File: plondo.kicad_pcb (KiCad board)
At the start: 2 copper layers, 126 parts, among them J1 AVR_TC2030, J2 USB4085, SW0 MX_SW_HS, SW1 MX_SW_HS, SW10 MX_SW_HS, SW11 MX_SW_HS, SW12 MX_SW_HS, SW13 MX_SW_HS, SW14 MX_SW_HS, SW15 MX_SW_HS, SW16 MX_SW_HS, SW17 MX_SW_HS, SW18 MX_SW_HS, SW19 MX_SW_HS, SW2 MX_SW_HS, SW20 MX_SW_HS, SW21 MX_SW_HS, SW22 MX_SW_HS, SW23 MX_SW_HS, SW24 MX_SW_HS, SW25 MX_SW_HS, SW26 MX_SW_HS, SW27 MX_SW_HS, SW28 MX_SW_HS, SW29 MX_SW_HS, SW3 MX_SW_HS, SW30 MX_SW_HS, SW31 MX_SW_HS, SW32 MX_SW_HS, SW33 MX_SW_HS, SW34 MX_SW_HS, SW35 MX_SW_HS, SW36 MX_SW_HS, SW37 MX_SW_HS, SW38 MX_SW_HS, SW39 MX_SW_HS, SW4 MX_SW_HS, SW40 MX_SW_HS, SW41 MX_SW_HS, SW42 MX_SW_HS, SW43 MX_SW_HS, SW44 MX_SW_HS, SW45 MX_SW_HS, SW46 MX_SW_HS, SW47 MX_SW_HS, SW5 MX_SW_HS, SW6 MX_SW_HS, SW7 MX_SW_HS, SW8 MX_SW_HS, SW9 MX_SW_HS, U1 ATmega32A-P, Y1 Crystal

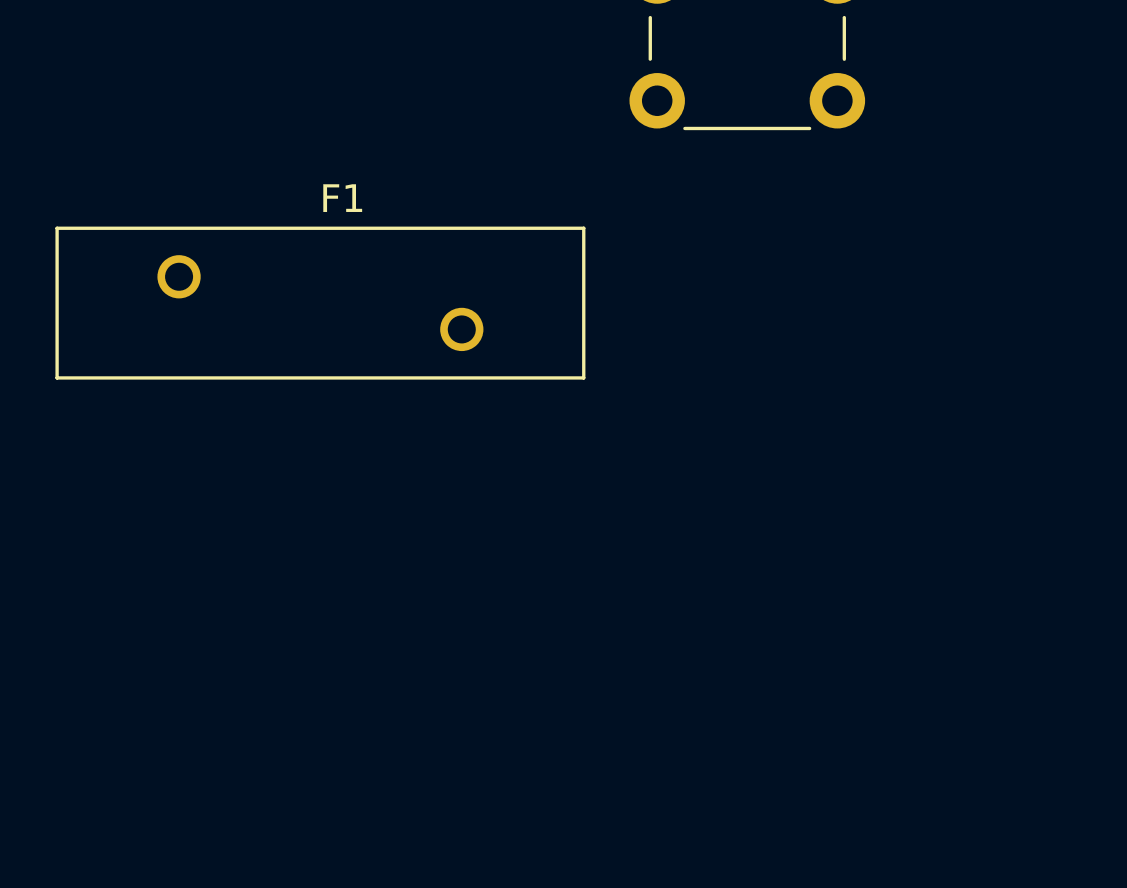
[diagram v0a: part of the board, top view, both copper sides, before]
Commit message: add pullups for i2c lines
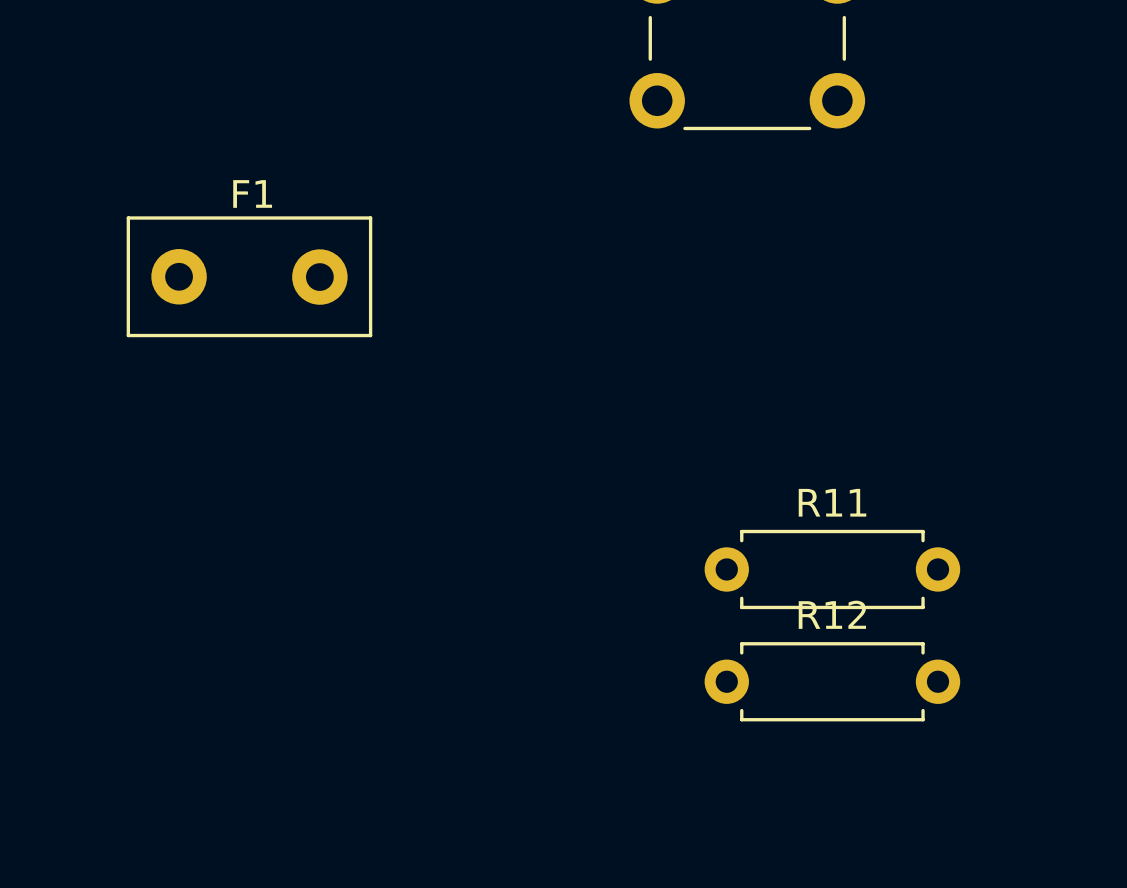
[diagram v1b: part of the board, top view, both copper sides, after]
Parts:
- added R11: 10k, Resistor_THT:R_Axial_DIN0207_L6.3mm_D2.5mm_P7.62mm_Horizontal, F.Cu at (-38.1, 114.3)
- added R12: 10k, Resistor_THT:R_Axial_DIN0207_L6.3mm_D2.5mm_P7.62mm_Horizontal, F.Cu at (-38.1, 118.3)
- F1: footprint Fuse:Fuse_BelFuse_0ZRE0100FF_L18.7mm_W5.1mm -> Fuse:Fuse_Littelfuse_395Series
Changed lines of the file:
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@@
     )
   )
+  (footprint "Resistor_THT:R_Axial_DIN0207_L6.3mm_D2.5mm_P7.62mm_Horizontal" (layer "F.Cu")
+    (at -38.1 114.3)
+    (descr "Resistor, Axial_DIN0207 series, Axial, Horizontal, pin pitch=7.62mm, 0.25W = 1/4W, length*diameter=6.3*2.5mm^2, http://cdn-reichelt.de/documents/datenblatt/B400/1_4W%23YAG.pdf")
+    (tags "Resistor Axial_DIN0207 series Axial Horizontal pin pitch 7.62mm 0.25W = 1/4W length 6.3mm diameter 2.5mm")
+    (property "Sheetfile" "plondo.kicad_sch")
+    (property "Sheetname" "")
+    (attr through_hole)
+    (fp_text reference "R11" (at 3.81 -2.37) (layer "F.SilkS")
+      (effects (font (size 1 1) (thickness 0.15)))
+    )
+    (fp_text value "10k" (at 3.81 2.37) (layer "F.Fab")
+      (effects (font (size 1 1) (thickness 0.15)))
+    )
+    (fp_text user "${REFERENCE}" (at 3.81 0) (layer "F.Fab")
+      (effects (font (size 1 1) (thickness 0.15)))
+    )
+    (fp_line (start 7.08 1.37) (end 7.08 1.04) (layer "F.SilkS") (width 0.12))
+    (fp_line (start 0.54 -1.04) (end 0.54 -1.37) (layer "F.SilkS") (width 0.12))
+    (fp_line (start 0.54 1.04) (end 0.54 1.37) (layer "F.SilkS") (width 0.12))
+    (fp_line (start 7.08 -1.37) (end 7.08 -1.04) (layer "F.SilkS") (width 0.12))
+    (fp_line (start 0.54 1.37) (end 7.08 1.37) (layer "F.SilkS") (width 0.12))
+    (fp_line (start 0.54 -1.37) (end 7.08 -1.37) (layer "F.SilkS") (width 0.12))
+    (fp_line (start 8.67 -1.5) (end -1.05 -1.5) (layer "F.CrtYd") (width 0.05))
+    (fp_line (start -1.05 1.5) (end 8.67 1.5) (layer "F.CrtYd") (width 0.05))
+    (fp_line (start 8.67 1.5) (end 8.67 -1.5) (layer "F.CrtYd") (width 0.05))
+    (fp_line (start -1.05 -1.5) (end -1.05 1.5) (layer "F.CrtYd") (width 0.05))
+    (fp_line (start 6.96 -1.25) (end 0.66 -1.25) (layer "F.Fab") (width 0.1))
+    (fp_line (start 6.96 1.25) (end 6.96 -1.25) (layer "F.Fab") (width 0.1))
+    (fp_line (start 7.62 0) (end 6.96 0) (layer "F.Fab") (width 0.1))
+    (fp_line (start 0.66 -1.25) (end 0.66 1.25) (layer "F.Fab") (width 0.1))
+    (fp_line (start 0.66 1.25) (end 6.96 1.25) (layer "F.Fab") (width 0.1))
+    (fp_line (start 0 0) (end 0.66 0) (layer "F.Fab") (width 0.1))
+    (pad "1" thru_hole circle (at 0 0) (size 1.6 1.6) (drill 0.8) (layers *.Cu *.Mask)
+      (net 5 "VCC") (pintype "passive"))
+    (pad "2" thru_hole oval (at 7.62 0) (size 1.6 1.6) (drill 0.8) (layers *.Cu *.Mask)
+      (net 76 "SDA") (pintype "passive"))
+    (model "${KICAD6_3DMODEL_DIR}/Resistor_THT.3dshapes/R_Axial_DIN0207_L6.3mm_D2.5mm_P7.62mm_Horizontal.wrl"
+      (offset (xyz 0 0 0))
+      (scale (xyz 1 1 1))
+      (rotate (xyz 0 0 0))
+    )
+  )
   (footprint "Diode_THT:D_DO-35_SOD27_P7.62mm_Horizontal" (layer "F.Cu")
     (at 137.16 45.72 -90)
@@
     )
   )
+  (footprint "Resistor_THT:R_Axial_DIN0207_L6.3mm_D2.5mm_P7.62mm_Horizontal" (layer "F.Cu")
+    (at -38.1 118.35)
+    (descr "Resistor, Axial_DIN0207 series, Axial, Horizontal, pin pitch=7.62mm, 0.25W = 1/4W, length*diameter=6.3*2.5mm^2, http://cdn-reichelt.de/documents/datenblatt/B400/1_4W%23YAG.pdf")
+    (tags "Resistor Axial_DIN0207 series Axial Horizontal pin pitch 7.62mm 0.25W = 1/4W length 6.3mm diameter 2.5mm")
+    (property "Sheetfile" "plondo.kicad_sch")
+    (property "Sheetname" "")
+    (attr through_hole)
+    (fp_text reference "R12" (at 3.81 -2.37) (layer "F.SilkS")
+      (effects (font (size 1 1) (thickness 0.15)))
+    )
+    (fp_text value "10k" (at 3.81 2.37) (layer "F.Fab")
+      (effects (font (size 1 1) (thickness 0.15)))
+    )
+    (fp_text user "${REFERENCE}" (at 3.81 0) (layer "F.Fab")
+      (effects (font (size 1 1) (thickness 0.15)))
+    )
+    (fp_line (start 7.08 1.37) (end 7.08 1.04) (layer "F.SilkS") (width 0.12))
+    (fp_line (start 0.54 -1.37) (end 7.08 -1.37) (layer "F.SilkS") (width 0.12))
+    (fp_line (start 0.54 1.04) (end 0.54 1.37) (layer "F.SilkS") (width 0.12))
+    (fp_line (start 7.08 -1.37) (end 7.08 -1.04) (layer "F.SilkS") (width 0.12))
+    (fp_line (start 0.54 -1.04) (end 0.54 -1.37) (layer "F.SilkS") (width 0.12))
+    (fp_line (start 0.54 1.37) (end 7.08 1.37) (layer "F.SilkS") (width 0.12))
+    (fp_line (start -1.05 1.5) (end 8.67 1.5) (layer "F.CrtYd") (width 0.05))
+    (fp_line (start 8.67 1.5) (end 8.67 -1.5) (layer "F.CrtYd") (width 0.05))
+    (fp_line (start -1.05 -1.5) (end -1.05 1.5) (layer "F.CrtYd") (width 0.05))
+    (fp_line (start 8.67 -1.5) (end -1.05 -1.5) (layer "F.CrtYd") (width 0.05))
+    (fp_line (start 0.66 1.25) (end 6.96 1.25) (layer "F.Fab") (width 0.1))
+    (fp_line (start 6.96 1.25) (end 6.96 -1.25) (layer "F.Fab") (width 0.1))
+    (fp_line (start 7.62 0) (end 6.96 0) (layer "F.Fab") (width 0.1))
+    (fp_line (start 0.66 -1.25) (end 0.66 1.25) (layer "F.Fab") (width 0.1))
+    (fp_line (start 0 0) (end 0.66 0) (layer "F.Fab") (width 0.1))
+    (fp_line (start 6.96 -1.25) (end 0.66 -1.25) (layer "F.Fab") (width 0.1))
+    (pad "1" thru_hole circle (at 0 0) (size 1.6 1.6) (drill 0.8) (layers *.Cu *.Mask)
+      (net 5 "VCC") (pintype "passive"))
+    (pad "2" thru_hole oval (at 7.62 0) (size 1.6 1.6) (drill 0.8) (layers *.Cu *.Mask)
+      (net 77 "SCL") (pintype "passive"))
+    (model "${KICAD6_3DMODEL_DIR}/Resistor_THT.3dshapes/R_Axial_DIN0207_L6.3mm_D2.5mm_P7.62mm_Horizontal.wrl"
+      (offset (xyz 0 0 0))
+      (scale (xyz 1 1 1))
+      (rotate (xyz 0 0 0))
+    )
+  )
   (footprint "Capacitor_THT:C_Disc_D7.5mm_W4.4mm_P5.00mm" (layer "F.Cu")
     (at -20.37 61.65)
@@
     )
   )
-  (footprint "Fuse:Fuse_BelFuse_0ZRE0100FF_L18.7mm_W5.1mm" (layer "F.Cu")
+  (footprint "Fuse:Fuse_Littelfuse_395Series" (layer "F.Cu")
     (at -57.86 103.74)
-    (descr "Fuse 0ZRE0100FF, BelFuse, Radial Leaded PTC,https://www.belfuse.com/resources/datasheets/circuitprotection/ds-cp-0zre-series.pdf")
-    (tags "0ZRE BelFuse radial PTC")
+    (descr "Fuse, TE5, Littelfuse/Wickmann, No. 460, No560,")
+    (tags "Fuse TE5 Littelfuse/Wickmann No. 460 No560 ")
     (property "Sheetfile" "plondo.kicad_sch")
     (property "Sheetname" "")
     (attr through_hole)
-    (fp_text reference "F1" (at 5.9 -2.8) (layer "F.SilkS")
+    (fp_text reference "F1" (at 2.65 -2.95) (layer "F.SilkS")
       (effects (font (size 1 1) (thickness 0.15)))
     )
-    (fp_text value "500mA" (at 5.6 5.2) (layer "F.Fab")
+    (fp_text value "500mA" (at 2.35 3.1) (layer "F.Fab")
       (effects (font (size 1 1) (thickness 0.15)))
     )
-    (fp_text user "${REFERENCE}" (at 5.7 0.4) (layer "F.Fab")
+    (fp_text user "${REFERENCE}" (at 2.75 -1.25) (layer "F.Fab")
       (effects (font (size 1 1) (thickness 0.15)))
     )
-    (fp_line (start -4.4 -1.75) (end -4.4 3.65) (layer "F.SilkS") (width 0.12))
-    (fp_line (start -4.4 3.65) (end 14.6 3.65) (layer "F.SilkS") (width 0.12))
-    (fp_line (start 14.6 -1.75) (end 14.6 3.65) (layer "F.SilkS") (width 0.12))
-    (fp_line (start -4.4 -1.75) (end 14.6 -1.75) (layer "F.SilkS") (width 0.12))
-    (fp_line (start -4.5 -1.85) (end 14.7 -1.85) (layer "F.CrtYd") (width 0.05))
-    (fp_line (start -4.5 3.75) (end 14.7 3.75) (layer "F.CrtYd") (width 0.05))
-    (fp_line (start -4.5 -1.85) (end -4.5 3.75) (layer "F.CrtYd") (width 0.05))
-    (fp_line (start 14.7 -1.85) (end 14.7 3.75) (layer "F.CrtYd") (width 0.05))
-    (fp_line (start -4.25 -1.6) (end -4.25 3.5) (layer "F.Fab") (width 0.1))
-    (fp_line (start -4.25 -1.6) (end 14.45 -1.6) (layer "F.Fab") (width 0.1))
-    (fp_line (start -4.25 3.5) (end 14.45 3.5) (layer "F.Fab") (width 0.1))
-    (fp_line (start 14.45 -1.6) (end 14.45 3.5) (layer "F.Fab") (width 0.1))
-    (pad "1" thru_hole circle (at 0 0) (size 1.56 1.56) (drill 1.01) (layers *.Cu *.Mask)
+    (fp_line (start 6.91 2.12) (end 6.91 -2.12) (layer "F.SilkS") (width 0.12))
+    (fp_line (start -1.83 -2.12) (end -1.83 2.12) (layer "F.SilkS") (width 0.12))
+    (fp_line (start -1.83 -2.12) (end 6.91 -2.12) (layer "F.SilkS") (width 0.12))
+    (fp_line (start 6.91 2.12) (end -1.83 2.12) (layer "F.SilkS") (width 0.12))
+    (fp_line (start 7.04 2.25) (end 7.04 -2.25) (layer "F.CrtYd") (width 0.05))
+    (fp_line (start -1.96 -2.25) (end -1.96 2.25) (layer "F.CrtYd") (width 0.05))
+    (fp_line (start -1.96 -2.25) (end 7.04 -2.25) (layer "F.CrtYd") (width 0.05))
+    (fp_line (start 7.04 2.25) (end -1.96 2.25) (layer "F.CrtYd") (width 0.05))
+    (fp_line (start -1.71 -2) (end -1.71 2) (layer "F.Fab") (width 0.1))
+    (fp_line (start 6.79 2) (end 6.79 -2) (layer "F.Fab") (width 0.1))
+    (fp_line (start 6.79 -2) (end -1.71 -2) (layer "F.Fab") (width 0.1))
+    (fp_line (start -1.71 2) (end 6.79 2) (layer "F.Fab") (width 0.1))
+    (pad "1" thru_hole circle (at 0 0) (size 2 2) (drill 1) (layers *.Cu *.Mask)
       (net 60 "Net-(F1-Pad1)") (pintype "passive"))
-    (pad "2" thru_hole circle (at 10.2 1.9) (size 1.56 1.56) (drill 1.01) (layers *.Cu *.Mask)
+    (pad "2" thru_hole circle (at 5.08 0.01) (size 2 2) (drill 1) (layers *.Cu *.Mask)
       (net 5 "VCC") (pintype "passive"))
-    (model "${KICAD6_3DMODEL_DIR}/Fuse.3dshapes/Fuse_BelFuse_0ZRE_0ZRE0100FF_L18.7mm_W5.1mm.wrl"
+    (model "${KICAD6_3DMODEL_DIR}/Fuse.3dshapes/Fuse_Littelfuse_395Series.wrl"
       (offset (xyz 0 0 0))
       (scale (xyz 1 1 1))

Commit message: edited schematics for clarity, position more of pcb
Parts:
- moved F1 308.8 mm to (246.4, 50.8), turned to 90 degrees
- moved C5 275.7 mm to (232.4, 45.8), turned to -90 degrees
- moved C3 273.0 mm to (241.3, 48.3), turned to 90 degrees
- moved J2 263.8 mm to (243.8, 39.6)
- moved C4 244.1 mm to (236.2, 50.8), turned to 90 degrees
- moved BSW1 235.8 mm to (183.4, 19.3)
- moved Y1 220.8 mm to (180.3, 38.1)
- moved RSW1 211.9 mm to (172.0, 19.3)
- moved C2 211.9 mm to (190.5, 40.6), turned to 90 degrees
- moved C1 209.1 mm to (175.3, 35.6), turned to -90 degrees
- moved D48 47.0 mm to (221.0, 47.0), turned to -90 degrees
- moved D49 44.5 mm to (218.4, 47.0), turned to -90 degrees
- moved U1 30.5 mm to (212.1, 43.2)

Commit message: position all components on the pcb
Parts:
- J1: value AVR_TC2030 -> AVR ISP
- moved R3 271.4 mm to (240.0, 62.2)
- moved R6 260.1 mm to (215.9, 54.6)
- moved R4 259.6 mm to (215.9, 47.0)
- moved R5 248.4 mm to (215.9, 50.8)
- moved R2 247.9 mm to (240.0, 58.4)
- moved R1 212.2 mm to (179.1, 33.0)
- moved J1 179.1 mm to (163.8, 35.6), turned to 90 degrees
- moved R12 127.3 mm to (59.7, 36.8)
- moved R11 122.4 mm to (59.7, 40.6)
- moved OL1 102.5 mm to (72.4, 41.9), turned to 90 degrees
- moved R9 90.9 mm to (45.7, 41.9), turned to 90 degrees
- moved R7 86.9 mm to (35.6, 41.9), turned to 90 degrees
- moved R10 75.0 mm to (50.8, 41.9), turned to 90 degrees
- moved LED2 74.9 mm to (40.6, 31.8), turned to 90 degrees
- moved R8 73.5 mm to (40.6, 41.9), turned to 90 degrees
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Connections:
- net XTAL1 renamed Net-(U1-Pad13)
- net XTAL2 renamed Net-(U1-Pad12)

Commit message: rearrange pins + misc pcb arrangement fixes
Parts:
- added Ref**: Val**, kbd:spacer_m2, F.Cu at (48.3, 83.8)
- added Ref**: Val**, kbd:spacer_m2, F.Cu at (251.5, 83.8)
- added Ref**: Val**, kbd:spacer_m2, F.Cu at (251.5, 124.5)
- added Ref**: Val**, kbd:spacer_m2, F.Cu at (48.3, 124.5)
- J1: footprint Connector_PinHeader_1.27mm:PinHeader_2x03_P1.27mm_Vertical -> Connector_PinHeader_2.54mm:PinHeader_2x03_P2.54mm_Vertical
- OL1: footprint kbd:OLED_1side -> kbd:OLED_v2
- SW0, SW1, SW10, SW11, SW12, SW13, SW14, SW15, SW16, SW17, SW18, SW19, SW2, SW20, SW21, SW22, SW23, SW24, SW25, SW26, SW27, SW28, SW29, SW3, SW30, SW31, SW32, SW33, SW34, SW35, SW36, SW37, SW38, SW39, SW4, SW40, SW41, SW42, SW43, SW44, SW45, SW46, SW47, SW5, SW6, SW7, SW8, SW9: moved to B.Cu
- Y1: value Crystal -> 16MHz
- moved LED1 202.0 mm to (236.2, 55.2), turned to 180 degrees
- moved R7 185.9 mm to (221.0, 55.9), turned to 0 degrees
- moved R8 124.7 mm to (165.1, 49.5), turned to 180 degrees
- moved R9 119.9 mm to (165.1, 52.7), turned to 180 degrees
- moved R10 115.2 mm to (165.1, 55.9), turned to 180 degrees
- moved BSW1 57.8 mm to (157.4, 35.2)
- moved RSW1 57.8 mm to (146.0, 35.2)
- moved J1 42.7 mm to (206.4, 38.7)
- moved D48 27.9 mm to (223.5, 40.6), turned to 90 degrees
- moved D49 23.9 mm to (226.7, 40.6), turned to 90 degrees
- moved R1 19.3 mm to (165.1, 46.4), turned to 180 degrees
- moved LED2 9.52 mm to (40.6, 41.3), turned to 180 degrees
- moved LED3 9.52 mm to (45.7, 41.3), turned to 180 degrees
- moved LED4 9.52 mm to (50.8, 41.3), turned to 180 degrees
- moved R2 7.24 mm to (241.9, 51.4), turned to -90 degrees
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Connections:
- ROT1 pad A: ROT_CLK -> ROT_A
- ROT1 pad B: ROT_DT -> ROT_B
- U1 pad 1: COL3 -> D+
- U1 pad 14: IND1 -> COL11
- U1 pad 15: IND2 -> unconnected-(U1-Pad15)
- U1 pad 16: IND3 -> unconnected-(U1-Pad16)
- U1 pad 17: unconnected-(U1-Pad17) -> BOOT
- U1 pad 18: unconnected-(U1-Pad18) -> IND1
- U1 pad 19: D+ -> IND2
- U1 pad 2: COL4 -> D-
- U1 pad 20: D- -> IND3
- U1 pad 21: BOOT -> ROW1
- U1 pad 24: COL8 -> ROW2
- U1 pad 25: COL9 -> ROW3
- U1 pad 26: COL10 -> ROW4
- U1 pad 27: COL11 -> COL0
- U1 pad 28: ROT_CLK -> COL1
- U1 pad 29: ROT_DT -> COL2
- U1 pad 3: COL5 -> ROT_A
- U1 pad 33: COL2 -> COL3
- U1 pad 34: COL1 -> COL4
- U1 pad 35: COL0 -> COL5
- U1 pad 36: ROW4 -> COL6
- U1 pad 37: ROW3 -> COL7
- U1 pad 38: ROW2 -> COL8
- U1 pad 39: ROW1 -> COL9
- U1 pad 4: COL6 -> ROT_B
- U1 pad 40: ROW0 -> COL10
- U1 pad 5: COL7 -> ROW0
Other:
- board outline added: 242.6 x 113.7 mm

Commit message: bunch of routing done
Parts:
- moved C4 5.00 mm to (200.7, 35.0), turned to -90 degrees
- moved R11 3.43 mm to (59.7, 37.8)
- moved R12 2.92 mm to (59.7, 41.0)
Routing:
- net GND: track 0.00 -> 180.9 mm, vias 0 -> 2
- net ROW4: track 0.00 -> 154.2 mm, vias 0 -> 1
- net IND1: track 0.00 -> 150.8 mm
- net ROW3: track 0.00 -> 148.6 mm, vias 0 -> 1
- net ROW2: track 0.00 -> 142.8 mm
- net IND2: track 0.00 -> 142.5 mm
- net IND3: track 0.00 -> 133.8 mm
- net VCC: track 0.00 -> 131.8 mm, vias 0 -> 1
- net ROW1: track 0.00 -> 130.4 mm
- net Net-(LED2-Pad1): track 0.00 -> 128.2 mm
- net Net-(LED3-Pad1): track 0.00 -> 124.8 mm
- net Net-(D41-Pad2): track 0.00 -> 123.1 mm, vias 0 -> 1
- net SDA: track 0.00 -> 121.0 mm
- net Net-(LED4-Pad1): track 0.00 -> 120.6 mm
- net SCL: track 0.00 -> 116.8 mm
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
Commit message: finish connecting rows to diodes
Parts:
- moved D0 1.27 mm to (40.6, 52.1)
- moved D1 1.27 mm to (50.8, 52.1)
- moved D10 1.27 mm to (142.2, 52.1)
- moved D11 1.27 mm to (152.4, 52.1)
- moved D12 1.27 mm to (38.1, 50.8)
- moved D13 1.27 mm to (48.3, 50.8)
- moved D14 1.27 mm to (58.4, 50.8)
- moved D15 1.27 mm to (68.6, 50.8)
- moved D16 1.27 mm to (78.7, 50.8)
- moved D17 1.27 mm to (88.9, 50.8)
- moved D18 1.27 mm to (99.1, 50.8)
- moved D19 1.27 mm to (109.2, 50.8)
- moved D2 1.27 mm to (61.0, 52.1)
- moved D20 1.27 mm to (119.4, 50.8)
- moved D21 1.27 mm to (129.5, 50.8)
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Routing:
- net Net-(D47-Pad2): track 0.00 -> 184.5 mm, vias 0 -> 1
- net Net-(D46-Pad2): track 0.00 -> 175.1 mm, vias 0 -> 1
- net Net-(D45-Pad2): track 0.00 -> 165.1 mm, vias 0 -> 1
- net Net-(D35-Pad2): track 0.00 -> 163.2 mm, vias 0 -> 1
- net Net-(D44-Pad2): track 0.00 -> 157.1 mm, vias 0 -> 2
- net Net-(D34-Pad2): track 0.00 -> 151.4 mm, vias 0 -> 1
- net Net-(D43-Pad2): track 0.00 -> 146.3 mm, vias 0 -> 1
- net Net-(D33-Pad2): track 0.00 -> 141.4 mm, vias 0 -> 1
- net Net-(D23-Pad2): track 0.00 -> 137.5 mm, vias 0 -> 1
- net Net-(D42-Pad2): track 0.00 -> 133.5 mm, vias 0 -> 1
- net Net-(D32-Pad2): track 0.00 -> 133.2 mm, vias 0 -> 2
- net Net-(D22-Pad2): track 0.00 -> 127.9 mm, vias 0 -> 1
- net Net-(D31-Pad2): track 0.00 -> 122.6 mm, vias 0 -> 1
- net Net-(D11-Pad2): track 0.00 -> 120.6 mm
- net Net-(D21-Pad2): track 0.00 -> 118.2 mm, vias 0 -> 1
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
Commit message: start redoing my awful routing
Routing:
- net Net-(D47-Pad2): track 184.5 -> 0.00 mm, vias 1 -> 0
- net Net-(D46-Pad2): track 175.1 -> 0.00 mm, vias 1 -> 0
- net GND: track 184.5 -> 16.5 mm, vias 2 -> 0
- net Net-(D35-Pad2): track 163.2 -> 0.00 mm, vias 1 -> 0
- net Net-(D34-Pad2): track 151.4 -> 0.00 mm, vias 1 -> 0
- net IND1: track 150.8 -> 0.00 mm
- net IND2: track 142.5 -> 0.00 mm
- net Net-(D23-Pad2): track 137.5 -> 0.00 mm, vias 1 -> 0
- net VCC: track 135.2 -> 0.00 mm, vias 1 -> 0
- net IND3: track 133.8 -> 0.00 mm
- net Net-(LED2-Pad1): track 128.2 -> 0.00 mm
- net Net-(D22-Pad2): track 127.9 -> 0.00 mm, vias 1 -> 0
- net Net-(LED3-Pad1): track 124.8 -> 0.00 mm
- net SDA: track 121.0 -> 0.00 mm
- net Net-(LED4-Pad1): track 120.6 -> 0.00 mm
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
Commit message: complete connecting key matrix
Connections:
- U1 pad 21: ROW1 -> ROW3
- U1 pad 24: ROW2 -> ROW4
- U1 pad 25: ROW3 -> ROW1
- U1 pad 26: ROW4 -> ROW2
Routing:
- net COL0: track 0.00 -> 219.6 mm
- net COL1: track 0.00 -> 201.9 mm
- net COL2: track 0.00 -> 186.9 mm
- net COL3: track 0.00 -> 177.5 mm
- net Net-(D47-Pad2): track 0.00 -> 175.8 mm, vias 0 -> 1
- net Net-(D46-Pad2): track 0.00 -> 166.5 mm, vias 0 -> 1
- net COL11: track 0.00 -> 166.2 mm
- net COL4: track 0.00 -> 158.2 mm
- net Net-(D35-Pad2): track 0.00 -> 151.9 mm, vias 0 -> 1
- net Net-(D34-Pad2): track 0.00 -> 142.8 mm, vias 0 -> 1
- net COL5: track 0.00 -> 140.4 mm
- net Net-(D23-Pad2): track 0.00 -> 135.5 mm, vias 0 -> 1
- net Net-(D11-Pad2): track 0.00 -> 135.4 mm, vias 0 -> 1
- net Net-(D10-Pad2): track 0.00 -> 129.2 mm, vias 0 -> 1
- net Net-(D22-Pad2): track 0.00 -> 125.6 mm, vias 0 -> 1
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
